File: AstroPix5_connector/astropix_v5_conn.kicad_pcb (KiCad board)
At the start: 4 copper layers, 56.4 x 65.6 mm, 51 parts, among them J1 HBOut, J10 SPI_right, J12 Measures_Analog, J14 Bias, J2 Conn_01x05, J3 pcie_GECCO, J4 HBOut, J5 HBOut, J7 HV_in_external, J8 Conn_01x03, J9 SPI_left, U2 AstroPix5_split_powerring

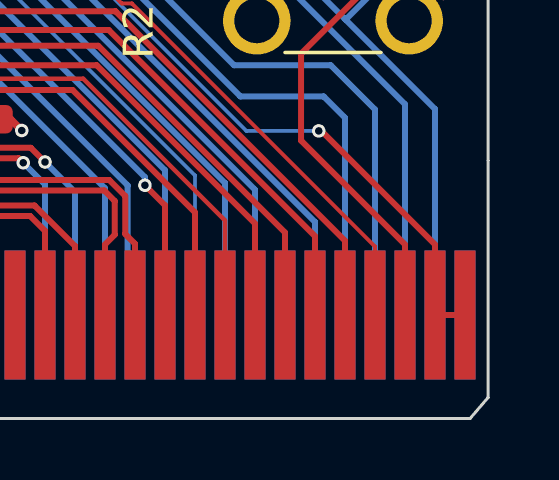
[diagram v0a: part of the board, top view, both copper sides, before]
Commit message: Fix duplicate SR_load in schematic + layout and adjust DigInj text in schematic
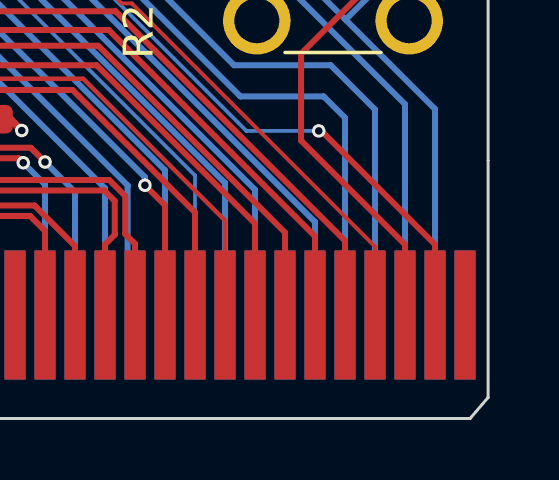
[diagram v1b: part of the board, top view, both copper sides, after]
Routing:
- net /SR_load: track 37.4 -> 36.4 mm
